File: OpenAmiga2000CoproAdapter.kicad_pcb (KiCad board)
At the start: 2 copper layers, 111.6 x 37.5 mm, 18 parts, among them CN1 A2000_COPRO_SLOT, P1 CONN_2, P10 CONN_1, P11 CONN_1, P12 CONN_1, P13 CONN_1, P14 CONN_1, P15 CONN_1, P2 CONN_2, P3 CONN_2, P4 CONN_2, P5 CONN_1, P6 CONN_1, P7 CONN_1, P8 CONN_1, P9 CONN_1, P99 OSHW_LOGO, U1 68000D

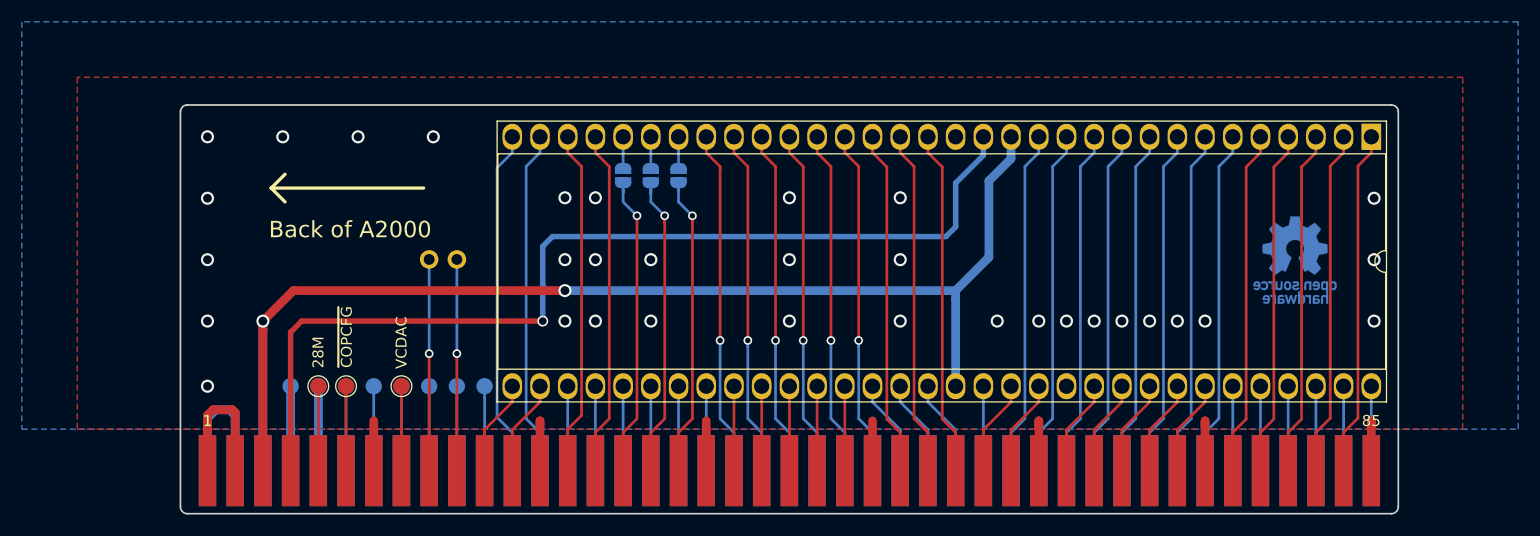
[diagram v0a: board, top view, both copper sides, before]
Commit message: Experiment arbitrating bus away from mainboard cpu
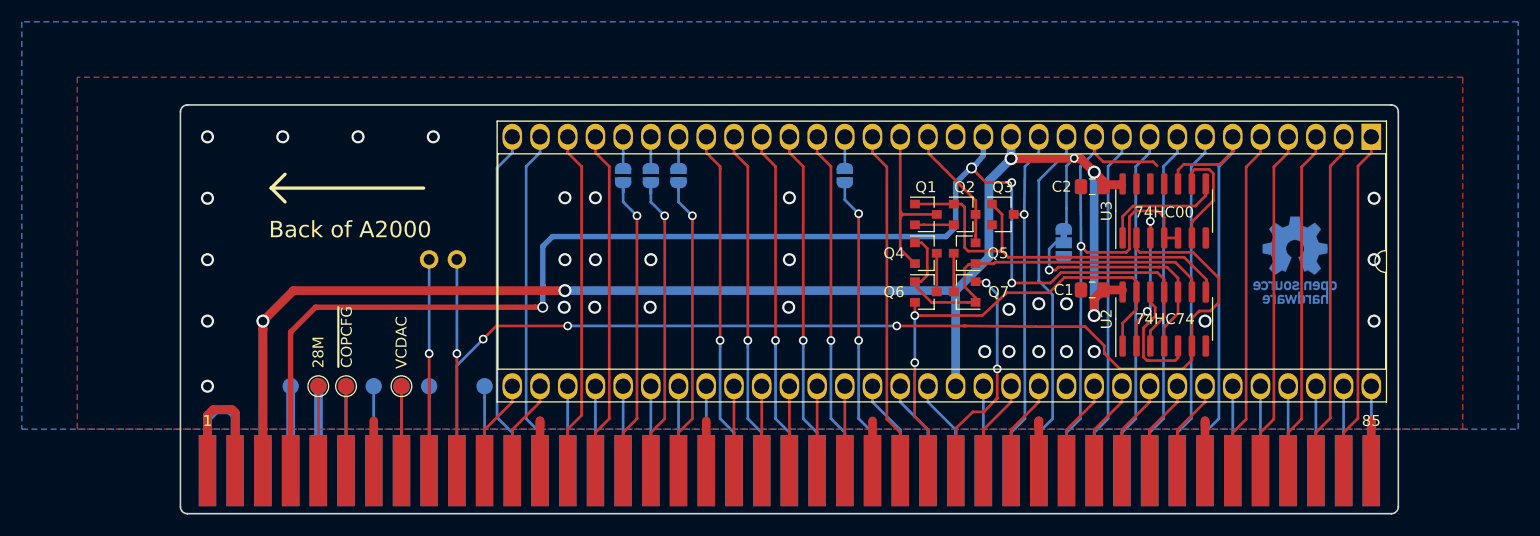
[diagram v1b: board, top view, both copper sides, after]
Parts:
- removed P12: CONN_1, TestPoint:TestPoint_Pad_D1.5mm
- added C1: C, Capacitor_SMD:C_0805_2012Metric_Pad1.15x1.40mm_HandSolder, F.Cu at (174.3, 126.2)
- added C2: C, Capacitor_SMD:C_0805_2012Metric_Pad1.15x1.40mm_HandSolder, F.Cu at (174.3, 116.7)
- added JP1: SolderJumper_3_Bridged12, Jumper:SolderJumper-3_P1.3mm_Bridged12_RoundedPad1.0x1.5mm, B.Cu at (171.7, 121.9)
- added JP2: SolderJumper_2_Open, Jumper:SolderJumper-2_P1.3mm_Open_RoundedPad1.0x1.5mm, B.Cu at (151.6, 115.7)
- added Q1: 2N7002, Package_TO_SOT_SMD:SOT-23, F.Cu at (159.1, 119.3)
- added Q2: 2N7002, Package_TO_SOT_SMD:SOT-23, F.Cu at (162.6, 119.3)
- added Q3: 2N7002, Package_TO_SOT_SMD:SOT-23, F.Cu at (166.1, 119.3)
- added Q4: 2N7002, Package_TO_SOT_SMD:SOT-23, F.Cu at (159.1, 122.8)
- added Q5: 2N7002, Package_TO_SOT_SMD:SOT-23, F.Cu at (162.6, 122.8)
- added Q6: 2N7002, Package_TO_SOT_SMD:SOT-23, F.Cu at (159.1, 126.4)
- added Q7: 2N7002, Package_TO_SOT_SMD:SOT-23, F.Cu at (162.6, 126.4)
- added U2: 74HC74, Package_SO:SOIC-14_3.9x8.7mm_P1.27mm, F.Cu at (180.9, 128.8)
- added U3: 74HC00, Package_SO:SOIC-14_3.9x8.7mm_P1.27mm, F.Cu at (180.9, 118.9)
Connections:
- CN1 pad 20: Net-(CN1-Pad20) -> /~BOSS
- U1 pad 17: /~hlt -> /~cpuhlt
- U1 pad 18: /~rst -> /~cpurst
- U1 pad 20: /e -> Net-(JP2-Pad2)
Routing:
- net /~BOSS: track 0.00 -> 99.5 mm, vias 0 -> 3
- net /BR: track 0.00 -> 38.7 mm
- net /~BR: track 0.00 -> 37.8 mm
- net +5V: track 117.1 -> 153.0 mm, vias 2 -> 6
- net /v7m: track 91.2 -> 125.6 mm, vias 1 -> 4
- net Net-(JP1-Pad2): track 0.00 -> 23.1 mm, vias 0 -> 1
- net /~cbg: track 31.7 -> 54.0 mm, vias 0 -> 1
- net /~cpurst: track 0.00 -> 16.1 mm
- net Net-(U2-Pad2): track 0.00 -> 14.2 mm, vias 0 -> 2
- net /~rst: track 31.7 -> 45.4 mm, vias 0 -> 2
- net Net-(U3-Pad1): track 0.00 -> 11.6 mm
- net Net-(U2-Pad12): track 0.00 -> 11.6 mm
- net /~cpuhlt: track 0.00 -> 10.8 mm
- net /~hlt: track 31.7 -> 21.1 mm, vias 0 -> 2
- net Net-(U3-Pad6): track 0.00 -> 10.1 mm
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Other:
- board text added: "Arb"
- board text added: "NOTE: If no CPU in mainboard Close E jumper, set ARB jumper to off"
- board text added: "Proto"
- board text added: "off"
- board text added: "on"
- board text removed: "V3"
- board text removed: "~BOSS"
